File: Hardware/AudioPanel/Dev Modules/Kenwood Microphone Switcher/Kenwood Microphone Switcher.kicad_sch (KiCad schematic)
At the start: 145 parts, among them J101 Screw_Terminal_01x02, J104 JST-PH UART/I2C, J105 2.54mm, J106 2.54mm, J107 2.54mm, J108 2.54mm, U10 SN74LV595ARGYR, U101 74HC14, U102 QTPy SAMD21, U103 AZ1117-5.0, U106 TC7660, U107 SN74LV595ARGYR, U108 ADS7830, U11 SN74LV595ARGYR, U110 SN74LV595ARGYR, U111 SN74LV595ARGYR, U9 INA219AxDCN

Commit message: Finished most of microphone switcher circuit
I'm very happy with where this is right now, I don't see anything immediately out of place and the schematic is now pretty well organized
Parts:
- removed C109: 22uF, Capacitor_SMD:C_0603_1608Metric, symbol Device:C_Small
- removed C117, C119, C121, C122, C124, C126, C128, C131, C132, C133, C134, C135: 0402, Capacitor_SMD:C_0402_1005Metric, symbol Device:C_Small
- removed C127, C144: 100nF, Capacitor_SMD:C_0402_1005Metric, symbol Device:C_Small
- removed D106, D107, D108, D109, D110, D112, D113, D114, D115, D116, D117, D118: WS2812B, Libraries:LED_WS2812B-2020_PLCC4_2.0x2.0mm, symbol LED:WS2812B-2020
- removed D111, D122, D123, D124: Green, LED_SMD:LED_0603_1608Metric, symbol Device:LED_Filled
- removed JP107, JP114, JP115, JP116: Jumper_2_Small_Open, Jumper:SolderJumper-2_P1.3mm_Open_Pad1.0x1.5mm, symbol Jumper:Jumper_2_Small_Open
- removed R112, R113: 220Ω, Resistor_SMD:R_0402_1005Metric, symbol Device:R_Small_US
- removed R114: 390, Resistor_SMD:R_0402_1005Metric, symbol Device:R_Small_US
- removed RN101: 47k, Resistor_SMD:R_Array_Convex_4x1206, symbol Library_MicSwitcher:R_Network04_Split
- removed U10, U107, U11, U110, U111: SN74LV595ARGYR, Libraries:RGY16_2P55X2P05, symbol 74xx:74HC595
- removed U101: 74HC14, Package_SO:SOIC-14_3.9x8.7mm_P1.27mm, symbol 74xx:74HC14
- removed U103: AZ1117-5.0, Package_TO_SOT_SMD:SOT-223-3_TabPin2, symbol Regulator_Linear:AZ1117-5.0
- added C112, C114: 22uF, Capacitor_SMD:C_0603_1608Metric, symbol Device:C_Small
- added C113, C115: 100nF, Capacitor_SMD:C_0402_1005Metric, symbol Device:C_Small
- added D105: Green, LED_SMD:LED_0603_1608Metric, symbol Device:LED_Filled
- added J107: 2.54mm, Connector_JST:JST_PH_S6B-PH-K_1x08_P2.00mm_Horizontal, symbol Connector_Generic:Conn_01x08
- added JP102, JP103, JP105, JP112: Jumper_2_Small_Open, Jumper:SolderJumper-2_P1.3mm_Open_Pad1.0x1.5mm, symbol Jumper:Jumper_2_Small_Open
- added R102: 3k, Resistor_SMD:R_0402_1005Metric, symbol Device:R_Small_US
- added R103, R107: 1k, Resistor_SMD:R_0402_1005Metric, symbol Device:R_Small_US
- added R106: 5k49, Resistor_SMD:R_0402_1005Metric, symbol Device:R_Small_US
- added R110: 330, Resistor_SMD:R_0402_1005Metric, symbol Device:R_Small_US
- added R118, R119, R122: 10k, Resistor_SMD:R_0402_1005Metric, symbol Device:R_Small_US
- added TP131, TP132, TP134, TP136, TP138, TP140, TP142, TP143: TestPoint_Flag, Libraries:KEYSTONE_5017, symbol Connector:TestPoint_Flag
- added U101, U103: TLV1117-ADJ, symbol Regulator_Linear:TLV1117-ADJ
- R113: renamed from R116; value 25k -> 10k
- R114: renamed from R117; value 25k -> 10k
- R115, R120, R121: value 390 -> 10k
- renumbered C116 to C101, C103 to C102, C113 to C103, C112 to C104, C110 to C105, C108 to C106, C101 to C107, C118 to C108, C120 to C109, C123 to C110, C125 to C111, C111 to C116, C115 to C117, C137 to C118, C139 to C119, C140 to C120, C102 to C121, C105 to C122, C136 to C123, C138 to C124, D15 to D101, D4 to D102, D3 to D103, D121 to D104, D105 to D106, D119 to D107, D101 to D108, F102 to F101, J105 to J101, J106 to J102, J107 to J103, J101 to J104, J108 to J105, J104 to J106, JP106 to JP101, JP108 to JP104, JP101 to JP106, JP102 to JP107, JP109 to JP108, JP103 to JP109, JP104 to JP110, JP77 to JP111, JP112 to JP114, JP105 to JP115, R103 to R101, R110 to R104, R6 to R105, R5 to R108, R106 to R109, R118 to R112, R101 to R116, R102 to R117, TP115 to TP101, TP122 to TP102, TP129 to TP103, TP136 to TP104, TP116 to TP105, TP123 to TP106, TP130 to TP107, TP137 to TP108, TP117 to TP109, TP124 to TP110, TP131 to TP111, TP138 to TP112, TP118 to TP113, TP125 to TP114, TP132 to TP115, TP139 to TP116, TP119 to TP117, TP126 to TP118, TP133 to TP119, TP140 to TP120, TP120 to TP121, TP127 to TP122, TP134 to TP123, TP141 to TP124, TP121 to TP125, TP128 to TP126, TP135 to TP127, TP142 to TP128, TP143 to TP129, TP144 to TP130, TP109 to TP133, TP110 to TP135, TP111 to TP137, TP112 to TP139, TP113 to TP141, TP114 to TP144, U106 to U102, U9 to U104, U108 to U105, U102 to U106
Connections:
- net +5V_MIC_480 is gone; now on net +5V: JP113.2 (B)
- net LED_700_PTT is gone; now on net SERIAL_MOSI: R120.1
- net LED_710_PTT is gone; now on net +5V_SAMD: R115.1
- net LED_EXTRA_PTT is gone; now on net SERIAL_LATCH: R121.1
- net +12_SENSE: now also C114.1, U101.3 (VI), U103.3 (VI)
- net +5V: now also C115.1, JP102.2 (B), JP103.2 (B), JP105.2 (B), JP112.2 (B), R102.2, U101.2 (VO); no longer JP113.1 (A)
- net +5V_595: now also R109.2
- net +8V: now also C112.1, C113.1, R106.2, U103.2 (VO)
- net GND: now also R120.2, R121.2, C112.2, C113.2, C114.2, C115.2, D105.1 (K), J107.8 (Pin_8), R103.2, R107.2, R118.2, R119.2, R122.2, TP143.1
- net SERIAL_LATCH: now also U106.1 (A0), J107.5 (Pin_5), TP138.1
- net SERIAL_SCLK: now also U106.9 (SCK), J107.3 (Pin_3), R118.1, TP134.1
- net at U102.7 (OSC): now also R104.1; no longer R104.2
- net at JP101.3 (B): now also R104.2; no longer R104.1
- net SERIAL_MISO: now reaches U106.10 (MI)
- net SERIAL_MISO: now also J107.4 (Pin_4), R119.1, TP136.1
- net SERIAL_MOSI: now reaches U106.11 (MO)
- net SERIAL_MOSI: now also J107.2 (Pin_2), TP132.1
- net PARALLEL_LOAD: now reaches U106.2 (A1)
- net PARALLEL_LOAD: now also J107.7 (Pin_7), R122.1, TP142.1
- net SERIAL_~{OE}: now reaches U106.3 (A2)
- net SERIAL_~{OE}: now also R115.2, J107.6 (Pin_6), TP140.1
- net SAMD_LED_UPDWN renamed SAMD_LED
- net SAMD_LED: now also J107.1 (Pin_1), TP131.1
- new net: R102.1, R103.1, U101.1 (ADJ)
- new net: D105.2 (A), R110.1
- new net: R106.1, R107.1, U103.1 (ADJ)
- new net +5V_165: JP112.1 (A), R110.2
- new net +5V_480: JP102.1 (A)
- new net +5V_700: JP105.1 (A)
- new net +5V_710: JP103.1 (A)
- new net +5V_EXTRA: JP113.1 (A)
- no-connect marks 4 -> 1
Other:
- added sheet LEDs (LEDs.kicad_sch)
- added sheet Output Error Detection (PISO.kicad_sch)
- added sheet SIPO Shift Registers (SIPO.kicad_sch)
- note added: "SAMD21 µC"
- note removed: "480 DOWN"
- note removed: "480 UP"
- note removed: "700 DOWN"
- note removed: "700 UP"
- note removed: "710 DOWN"
- note removed: "710 UP"
- note removed: "CODRIVER DOWN"
- note removed: "CODRIVER UP"
- note removed: "DRIVER DOWN"
- note removed: "DRIVER UP"
- note removed: "EXTRA DOWN"
- note removed: "EXTRA UP"
- note removed: "Keypad Button LEDs"
- note removed: "SAMD21 Microcontroller"
- note removed: "Serial-In/Parallel-Out"
- moved on the sheet: C101, C102, C103, C104, C105, C106, C108, C109, C110, C111, C116, C117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

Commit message: Isolated mic outputs to their respective radios
Button presses are easy to isolate with optocouplers, I'm coupling in the mic signals using dc blocking capacitors and generating the bias voltages from the respective radios
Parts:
- renumbered C107 to C101, C114 to C102, C102 to C103, C112 to C104, C121 to C105, C113 to C106, C122 to C107, C103 to C108, C117 to C109, C104 to C110, C105 to C111, C115 to C112, C106 to C113, C116 to C114, C101 to C115, C108 to C116, C109 to C117, C110 to C118, C111 to C119, C123 to C120, C118 to C121, C124 to C122, C119 to C123, C120 to C124, D106 to D102, D108 to D103, D103 to D105, D105 to D106, D102 to D107, D107 to D108, J104 to J101, J106 to J102, J107 to J103, J101 to J104, J102 to J105, J103 to J106, J105 to J107, JP106 to JP101, JP107 to JP102, JP109 to JP103, JP110 to JP104, JP115 to JP105, JP111 to JP106, JP101 to JP107, JP112 to JP108, JP104 to JP109, JP108 to JP110, JP102 to JP111, JP103 to JP112, JP105 to JP113, JP113 to JP114, JP114 to JP115, R116 to R101, R117 to R102, R101 to R103, R115 to R104, R121 to R105, R122 to R106, R106 to R107, R107 to R108, R102 to R109, R103 to R110, R109 to R112, R118 to R113, R108 to R114, R119 to R115, R120 to R116, R104 to R117, R110 to R118, R105 to R119, R113 to R120, R114 to R121, R112 to R122, TP133 to TP101, TP135 to TP102, TP137 to TP103, TP139 to TP104, TP141 to TP105, TP131 to TP106, TP132 to TP107, TP134 to TP108, TP136 to TP109, TP138 to TP110, TP140 to TP111, TP142 to TP112, TP143 to TP113, TP101 to TP114, TP105 to TP115, TP109 to TP116, TP113 to TP117, TP117 to TP118, TP121 to TP119, TP125 to TP120, TP102 to TP121, TP106 to TP122, TP110 to TP123, TP114 to TP124, TP118 to TP125, TP122 to TP126, TP126 to TP127, TP144 to TP128, TP103 to TP129, TP107 to TP130, TP111 to TP131, TP115 to TP132, TP119 to TP133, TP123 to TP134, TP127 to TP135, TP104 to TP136, TP108 to TP137, TP112 to TP138, TP116 to TP139, TP120 to TP140, TP124 to TP141, TP128 to TP142, TP129 to TP143, TP130 to TP144, U103 to U101, U101 to U102, U104 to U103, U106 to U104, U102 to U105, U105 to U106
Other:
- moved on the sheet: JP111, JP112, JP113, JP114

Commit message: Added labeling and organized pages
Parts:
- added TP106: TestPoint_Flag, Libraries:KEYSTONE_5017, symbol Connector:TestPoint_Flag
- J103: footprint Connector_JST:JST_PH_S6B-PH-K_1x08_P2.00mm_Horizontal -> Connector_JST:JST_PH_S6B-PH-K_1x10_P2.00mm_Horizontal; symbol Connector_Generic:Conn_01x08 -> Connector_Generic:Conn_01x10
- U101, U102: footprint (none) -> Libraries:YDC4
- renumbered TP106 to TP107, TP107 to TP108, TP108 to TP109, TP109 to TP110, TP110 to TP111, TP111 to TP112, TP112 to TP113, TP113 to TP114, TP114 to TP115, TP115 to TP116, TP116 to TP117, TP117 to TP118, TP118 to TP119, TP119 to TP120, TP120 to TP121, TP121 to TP122, TP122 to TP123, TP123 to TP124, TP124 to TP125, TP125 to TP126, TP126 to TP127, TP127 to TP128, TP128 to TP129, TP129 to TP130, TP130 to TP131, TP131 to TP132, TP132 to TP133, TP133 to TP134, TP134 to TP135, TP135 to TP136, TP136 to TP137, TP137 to TP138, TP138 to TP139, TP139 to TP140, TP140 to TP141, TP141 to TP142, TP142 to TP143, TP143 to TP144, TP144 to TP145
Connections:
- net GND: now also J103.10 (Pin_10); no longer J103.8 (Pin_8), TP114.1
- net PARALLEL_LOAD: now also J103.9 (Pin_9), TP114.1; no longer J103.7 (Pin_7), TP113.1
- net SAMD_LED: now also J103.3 (Pin_3), TP108.1; no longer J103.1 (Pin_1), TP107.1
- net SERIAL_LATCH: now also J103.7 (Pin_7), TP112.1; no longer J103.5 (Pin_5), TP111.1
- net SERIAL_MISO: now also J103.6 (Pin_6), TP111.1; no longer J103.4 (Pin_4), TP110.1
- net SERIAL_MOSI: now also J103.4 (Pin_4), TP109.1; no longer J103.2 (Pin_2), TP108.1
- net SERIAL_SCLK: now also J103.5 (Pin_5), TP110.1; no longer J103.3 (Pin_3), TP109.1
- net SERIAL_~{OE}: now also J103.8 (Pin_8), TP113.1; no longer J103.6 (Pin_6), TP112.1
- new net SERIAL_OUT: J103.1 (Pin_1), TP106.1
- new net SERIAL_~{CLEAR}: J103.2 (Pin_2), TP107.1
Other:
- note added: "Multi-Color LEDs"
- title: Kenwood Handset Switcher - Dev Board -> Kenwood Handset Switcher - Main Page
- moved on the sheet: C120, C121, C122, C123, C124, D108, JP101, JP102, JP103, JP104, JP115, R120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

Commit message: Improved switching logic
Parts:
- removed C115, C116, C118: 22uF, Capacitor_SMD:C_0603_1608Metric, symbol Device:C_Small
- removed C117, C119: 100nF, Capacitor_SMD:C_0402_1005Metric, symbol Device:C_Small
- removed D107: Green, LED_SMD:LED_0603_1608Metric, symbol Device:LED_Filled
- removed JP107, JP110: Jumper_3_Open, Libraries:SolderBridge_3L, symbol Jumper:Jumper_3_Open
- removed R117: 1k, Resistor_SMD:R_0402_1005Metric, symbol Device:R_Small_US
- removed R119: 330, Resistor_SMD:R_0402_1005Metric, symbol Device:R_Small_US
- removed U105: TC7660, Package_SO:SOIC-8_3.9x4.9mm_P1.27mm, symbol Converter_DCDC:TC7662Bx0A
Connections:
- no-connect marks 1 -> 0
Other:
- sheet Output Error Detection renamed PISO Shift Registers - 48bit
- sheet SIPO Shift Registers renamed SIPO Shift Registers - 48bit
- sheet 4x4 Crosspoint Switch ports: added none; removed VSS
- moved on the sheet: C101, C102, C103, C104, C106, C108, C110, C111, C112, C113, C114, D101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

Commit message: Added data lowpass filter stuffs
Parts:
- removed JP111, JP112, JP113, JP114: Jumper_2_Small_Open, Jumper:SolderJumper-2_P1.3mm_Open_Pad1.0x1.5mm, symbol Jumper:Jumper_2_Small_Open
- added D107, D109: Green, LED_SMD:LED_0603_1608Metric, symbol Device:LED_Filled
- added R117: 1k, Resistor_SMD:R_0402_1005Metric, symbol Device:R_Small_US
- added R119: 2k7, Resistor_SMD:R_0402_1005Metric, symbol Device:R_Small_US
- R112, R114, R118, R122: value 330 -> 1k
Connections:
- net +5V_CROSSPOINT: now also R117.2
- net +8V: now also D109.2 (A)
- net GND: now also D107.1 (K), R119.2
- new net: D109.1 (K), R119.1
- new net: D107.2 (A), R117.1
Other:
- sheet D-700 MIC Output ports: added none; removed +5V
- sheet D-710 MIC Output ports: added none; removed +5V
- sheet EXTRA MIC Output ports: added none; removed +5V
- sheet TS-480 MIC Output ports: added none; removed +5V
- moved on the sheet: C112, C114, D105, JP109, R114, U103

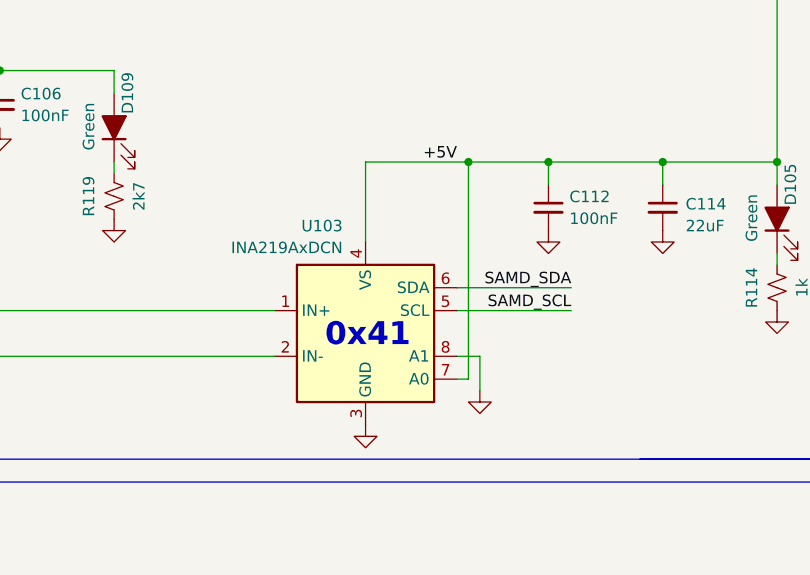
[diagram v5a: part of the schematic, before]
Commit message: Adjusted I2C addresses and component identifiers
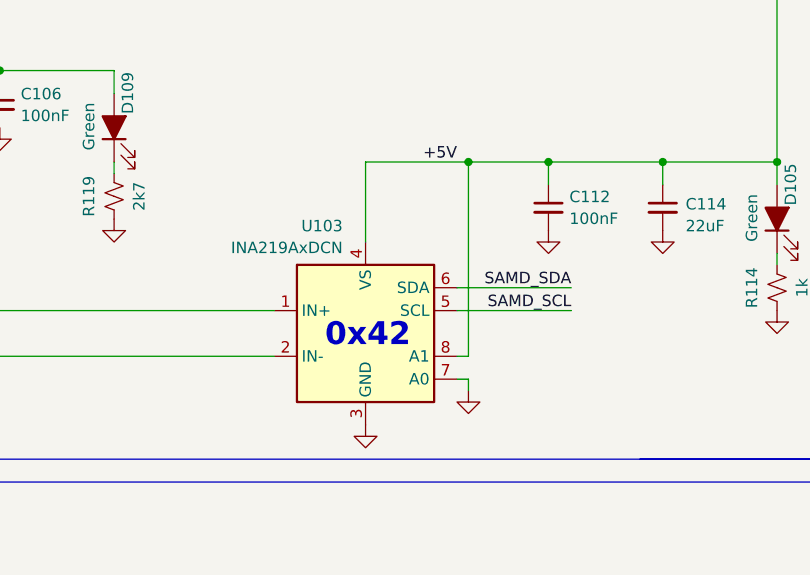
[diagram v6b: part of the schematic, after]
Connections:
- net +5V: now also U103.8 (A1); no longer U103.7 (A0)
- net GND: now also U103.7 (A0); no longer U103.8 (A1)
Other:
- note added: "0x42"
- note removed: "0x41"
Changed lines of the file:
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@@
 		)
 	)
-	(text "0x41"
+	(text "0x42"
 		(exclude_from_sim no)
 		(at 150.114 78.994 0)
@@
 	)
 	(junction
-		(at 161.29 59.69)
-		(diameter 0)
-		(color 0 0 0 0)
-	)
-	(junction
 		(at 234.95 91.44)
 		(diameter 0)
@@
 		(color 0 0 0 0)
 	)
+	(junction
+		(at 161.29 59.69)
+		(diameter 0)
+		(color 0 0 0 0)
+	)
 	(bus_entry
 		(at 281.94 241.3)
@@
 		)
 	)
+	(wire
+		(pts
+			(xy 161.29 59.69) (xy 170.18 59.69)
+		)
+		(stroke
+			(width 0)
+			(type default)
+		)
+	)
 	(bus
 		(pts
@@
 	(wire
 		(pts
-			(xy 160.02 81.28) (xy 162.56 81.28)
-		)
-		(stroke
-			(width 0)
-			(type default)
-		)
-	)
-	(wire
-		(pts
 			(xy 321.31 203.2) (xy 321.31 218.44)
 		)
@@
 	(wire
 		(pts
+			(xy 161.29 59.69) (xy 161.29 81.28)
+		)
+		(stroke
+			(width 0)
+			(type default)
+		)
+	)
+	(wire
+		(pts
 			(xy 140.97 147.32) (xy 157.48 147.32)
 		)
@@
 	(wire
 		(pts
-			(xy 161.29 59.69) (xy 170.18 59.69)
+			(xy 149.86 59.69) (xy 161.29 59.69)
 		)
 		(stroke
@@
 	(wire
 		(pts
-			(xy 149.86 59.69) (xy 161.29 59.69)
-		)
-		(stroke
-			(width 0)
-			(type default)
-		)
-	)
-	(wire
-		(pts
 			(xy 120.65 175.26) (xy 110.49 175.26)
 		)
@@
 		)
 	)
-	(wire
-		(pts
-			(xy 162.56 81.28) (xy 162.56 85.09)
-		)
-		(stroke
-			(width 0)
-			(type default)
-		)
-	)
 	(bus
 		(pts
@@
 		)
 	)
+	(wire
+		(pts
+			(xy 160.02 81.28) (xy 161.29 81.28)
+		)
+		(stroke
+			(width 0)
+			(type default)
+		)
+	)
 	(polyline
 		(pts
@@
 	(wire
 		(pts
+			(xy 161.29 83.82) (xy 160.02 83.82)
+		)
+		(stroke
+			(width 0)
+			(type default)
+		)
+	)
+	(wire
+		(pts
 			(xy 264.16 167.64) (xy 270.51 167.64)
 		)
@@
 	(wire
 		(pts
-			(xy 160.02 83.82) (xy 161.29 83.82)
-		)
-		(stroke
-			(width 0)
-			(type default)
-		)
-	)
-	(wire
-		(pts
 			(xy 182.88 144.78) (xy 189.23 144.78)
 		)
@@
 	(wire
 		(pts
-			(xy 161.29 59.69) (xy 161.29 83.82)
-		)
-		(stroke
-			(width 0)
-			(type default)
-		)
-	)
-	(wire
-		(pts
 			(xy 264.16 144.78) (xy 270.51 144.78)
 		)
@@
 		)
 	)
+	(wire
+		(pts
+			(xy 161.29 85.09) (xy 161.29 83.82)
+		)
+		(stroke
+			(width 0)
+			(type default)
+		)
+	)
 	(bus
 		(pts
@@
 	(symbol
 		(lib_id "power:GND")
-		(at 162.56 85.09 0)
+		(at 161.29 85.09 0)
 		(unit 1)
 		(exclude_from_sim no)
@@
 		(fields_autoplaced yes)
 		(property "Reference" "#PWR0121"
-			(at 162.56 91.44 0)
+			(at 161.29 91.44 0)
 			(effects
 				(font
@@
 		)
 		(property "Value" "GND"
-			(at 162.56 89.2231 0)
+			(at 161.29 89.2231 0)
 			(effects
 				(font
@@
 		)
 		(property "Footprint" ""
-			(at 162.56 85.09 0)
+			(at 161.29 85.09 0)
 			(effects
 				(font
@@
 		)
 		(property "Datasheet" ""
-			(at 162.56 85.09 0)
+			(at 161.29 85.09 0)
 			(effects
 				(font
@@
 		)
 		(property "Description" "Power symbol creates a global label with name \"GND\" , ground"
-			(at 162.56 85.09 0)
+			(at 161.29 85.09 0)
 			(effects
 				(font

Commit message: Small tweaks
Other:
- moved on the sheet: D107, JP109, R117

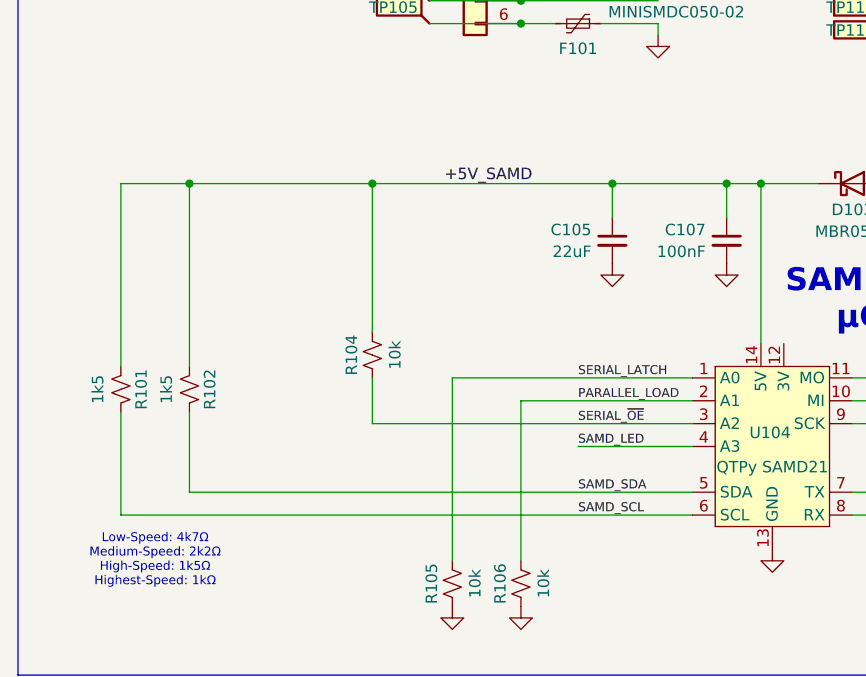
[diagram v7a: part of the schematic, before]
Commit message: Fixed pullup/dwn resistors, rotated optoisolator on MIC PTT outs
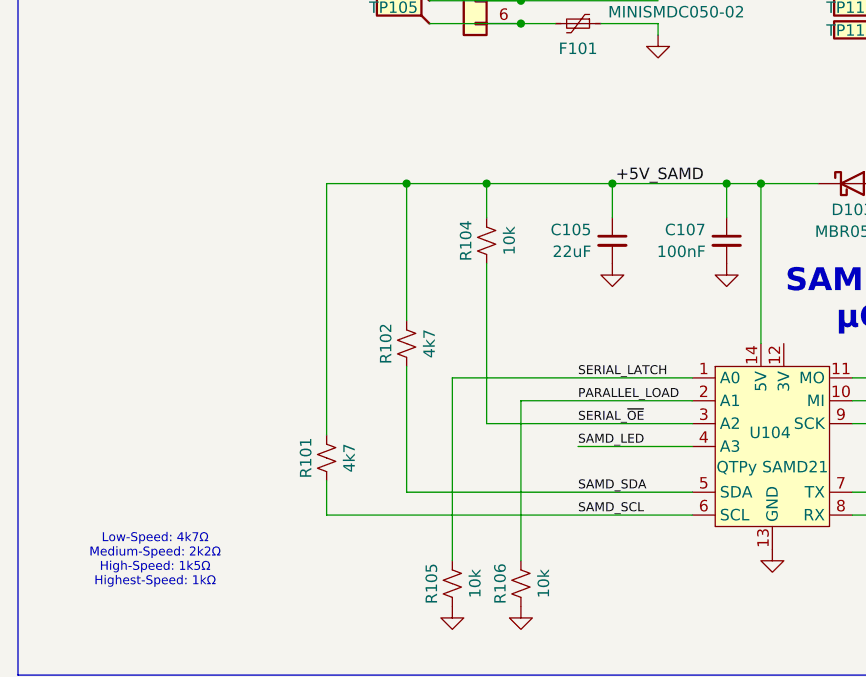
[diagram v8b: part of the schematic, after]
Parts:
- R101, R102: value 1k5 -> 4k7
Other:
- moved on the sheet: R101, R102, R104
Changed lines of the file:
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@@
 	)
 	(junction
-		(at 33.02 210.82)
-		(diameter 0)
-		(color 0 0 0 0)
-	)
-	(junction
 		(at 396.24 182.88)
 		(diameter 0)
@@
 	)
 	(junction
-		(at 53.34 210.82)
-		(diameter 0)
-		(color 0 0 0 0)
-	)
-	(junction
 		(at 322.58 33.02)
 		(diameter 0)
@@
 	)
 	(junction
+		(at 66.04 210.82)
+		(diameter 0)
+		(color 0 0 0 0)
+	)
+	(junction
 		(at 96.52 210.82)
 		(diameter 0)
@@
 	)
 	(junction
+		(at 57.15 210.82)
+		(diameter 0)
+		(color 0 0 0 0)
+	)
+	(junction
 		(at 398.78 43.18)
 		(diameter 0)
@@
 	(wire
 		(pts
+			(xy 66.04 210.82) (xy 80.01 210.82)
+		)
+		(stroke
+			(width 0)
+			(type default)
+		)
+	)
+	(wire
+		(pts
 			(xy 321.31 203.2) (xy 321.31 218.44)
 		)
@@
 	(wire
 		(pts
-			(xy 25.4 210.82) (xy 33.02 210.82)
-		)
-		(stroke
-			(width 0)
-			(type default)
-		)
-	)
-	(wire
-		(pts
 			(xy 161.29 59.69) (xy 161.29 81.28)
 		)
@@
 	(wire
 		(pts
-			(xy 53.34 237.49) (xy 53.34 232.41)
+			(xy 66.04 237.49) (xy 66.04 219.71)
 		)
 		(stroke
@@
 	(wire
 		(pts
-			(xy 25.4 210.82) (xy 25.4 231.14)
+			(xy 48.26 210.82) (xy 48.26 238.76)
 		)
 		(stroke
@@
 	(wire
 		(pts
+			(xy 66.04 210.82) (xy 57.15 210.82)
+		)
+		(stroke
+			(width 0)
+			(type default)
+		)
+	)
+	(wire
+		(pts
 			(xy 149.86 59.69) (xy 149.86 68.58)
 		)
@@
 	(wire
 		(pts
-			(xy 33.02 236.22) (xy 33.02 245.11)
+			(xy 57.15 231.14) (xy 57.15 245.11)
 		)
 		(stroke
@@
 	(wire
 		(pts
-			(xy 33.02 210.82) (xy 53.34 210.82)
-		)
-		(stroke
-			(width 0)
-			(type default)
-		)
-	)
-	(wire
-		(pts
 			(xy 340.36 143.51) (xy 353.06 143.51)
 		)
@@
 	(wire
 		(pts
+			(xy 66.04 214.63) (xy 66.04 210.82)
+		)
+		(stroke
+			(width 0)
+			(type default)
+		)
+	)
+	(wire
+		(pts
 			(xy 273.05 198.12) (xy 264.16 198.12)
 		)
@@
 	(wire
 		(pts
-			(xy 33.02 210.82) (xy 33.02 231.14)
+			(xy 57.15 210.82) (xy 57.15 226.06)
 		)
 		(stroke
@@
 	(wire
 		(pts
-			(xy 53.34 210.82) (xy 80.01 210.82)
-		)
-		(stroke
-			(width 0)
-			(type default)
-		)
-	)
-	(wire
-		(pts
 			(xy 182.88 144.78) (xy 189.23 144.78)
 		)
@@
 	(wire
 		(pts
+			(xy 48.26 210.82) (xy 57.15 210.82)
+		)
+		(stroke
+			(width 0)
+			(type default)
+		)
+	)
+	(wire
+		(pts
 			(xy 85.09 190.5) (xy 69.85 190.5)
 		)
@@
 	(wire
 		(pts
-			(xy 25.4 247.65) (xy 88.9 247.65)
+			(xy 48.26 247.65) (xy 88.9 247.65)
 		)
 		(stroke
@@
 	(wire
 		(pts
-			(xy 53.34 210.82) (xy 53.34 227.33)
-		)
-		(stroke
-			(width 0)
-			(type default)
-		)
-	)
-	(wire
-		(pts
 			(xy 337.82 220.98) (xy 354.33 220.98)
 		)
@@
 	(wire
 		(pts
-			(xy 33.02 245.11) (xy 88.9 245.11)
+			(xy 57.15 245.11) (xy 88.9 245.11)
 		)
 		(stroke
@@
 	(wire
 		(pts
-			(xy 53.34 237.49) (xy 88.9 237.49)
+			(xy 66.04 237.49) (xy 88.9 237.49)
 		)
 		(stroke
@@
 	(wire
 		(pts
-			(xy 25.4 236.22) (xy 25.4 247.65)
+			(xy 48.26 243.84) (xy 48.26 247.65)
 		)
 		(stroke
@@
 	)
 	(label "+5V_SAMD"
-		(at 71.12 210.82 180)
+		(at 90.17 210.82 180)
 		(effects
 			(font
@@
 	(symbol
 		(lib_id "Device:R_Small_US")
-		(at 33.02 233.68 0)
-		(mirror y)
+		(at 57.15 228.6 0)
 		(unit 1)
 		(exclude_from_sim no)
@@
 		(dnp no)
 		(property "Reference" "R102"
-			(at 35.306 233.68 90)
+			(at 54.864 228.6 90)
 			(effects
 				(font
@@
 			)
 		)
-		(property "Value" "1k5"
-			(at 30.48 233.68 90)
+		(property "Value" "4k7"
+			(at 59.69 228.6 90)
 			(effects
 				(font
@@
 		)
 		(property "Footprint" "Resistor_SMD:R_0402_1005Metric"
-			(at 33.02 233.68 0)
+			(at 57.15 228.6 0)
 			(effects
 				(font
@@
 		)
 		(property "Datasheet" "~"
-			(at 33.02 233.68 0)
+			(at 57.15 228.6 0)
 			(effects
 				(font
@@
 		)
 		(property "Description" "Resistor, small US symbol"
-			(at 33.02 233.68 0)
+			(at 57.15 228.6 0)
 			(effects
 				(font
@@
 	(symbol
 		(lib_id "Device:R_Small_US")
-		(at 53.34 229.87 0)
+		(at 66.04 217.17 0)
 		(unit 1)
 		(exclude_from_sim no)
@@
 		(dnp no)
 		(property "Reference" "R104"
-			(at 51.054 229.87 90)
+			(at 63.754 217.17 90)
 			(effects
 				(font
@@
 		)
 		(property "Value" "10k"
-			(at 55.88 229.87 90)
+			(at 68.58 217.17 90)
 			(effects
 				(font
@@
 		)
 		(property "Footprint" "Resistor_SMD:R_0402_1005Metric"
-			(at 53.34 229.87 0)
+			(at 66.04 217.17 0)
 			(effects
 				(font
@@
 		)
 		(property "Datasheet" "~"
-			(at 53.34 229.87 0)
+			(at 66.04 217.17 0)
 			(effects
 				(font
@@
 		)
 		(property "Description" "Resistor, small US symbol"
-			(at 53.34 229.87 0)
+			(at 66.04 217.17 0)
 			(effects
 				(font
@@
 	(symbol
 		(lib_id "Device:R_Small_US")
-		(at 25.4 233.68 0)
-		(mirror y)
+		(at 48.26 241.3 0)
 		(unit 1)
 		(exclude_from_sim no)
@@
 		(dnp no)
 		(property "Reference" "R101"
-			(at 27.686 233.68 90)
+			(at 45.974 241.3 90)
 			(effects
 				(font
@@
 			)
 		)
-		(property "Value" "1k5"
-			(at 22.86 233.68 90)
+		(property "Value" "4k7"
+			(at 50.8 241.3 90)
 			(effects
 				(font
@@
 		)
 		(property "Footprint" "Resistor_SMD:R_0402_1005Metric"
-			(at 25.4 233.68 0)
+			(at 48.26 241.3 0)
 			(effects
 				(font
@@
 		)
 		(property "Datasheet" "~"
-			(at 25.4 233.68 0)
+			(at 48.26 241.3 0)
 			(effects
 				(font
@@
 		)
 		(property "Description" "Resistor, small US symbol"
-			(at 25.4 233.68 0)
+			(at 48.26 241.3 0)
 			(effects
 				(font
